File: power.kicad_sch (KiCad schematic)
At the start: 13 parts, among them J2 USB_C_Receptacle_PowerOnly_6P

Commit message: Add files via upload
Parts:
- C1, C2, C3, C4: footprint (none) -> Capacitor_SMD:C_0805_2012Metric
- D2: footprint (none) -> LED_SMD:LED_0805_2012Metric
- R1, R2: footprint (none) -> Resistor_SMD:R_0603_1608Metric
- R3: footprint (none) -> Resistor_SMD:R_0805_2012Metric
- R4: value 2K -> 1.5K; footprint (none) -> Resistor_SMD:R_0805_2012Metric
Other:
- moved on the sheet: D2, R4
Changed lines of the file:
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@@
 	(wire
 		(pts
-			(xy 130.81 90.17) (xy 132.08 90.17)
+			(xy 130.81 69.85) (xy 132.08 69.85)
 		)
 		(stroke
@@
 	(wire
 		(pts
-			(xy 147.32 66.04) (xy 147.32 90.17)
+			(xy 147.32 66.04) (xy 147.32 69.85)
 		)
 		(stroke
@@
 	(wire
 		(pts
-			(xy 130.81 67.31) (xy 130.81 90.17)
+			(xy 130.81 67.31) (xy 130.81 69.85)
 		)
 		(stroke
@@
 			)
 		)
-		(property "Footprint" ""
+		(property "Footprint" "Capacitor_SMD:C_0805_2012Metric"
 			(at 156.21 65.0748 0)
 			(effects
@@
 	(symbol
 		(lib_id "Device:R")
-		(at 135.89 90.17 90)
+		(at 135.89 69.85 90)
 		(unit 1)
 		(exclude_from_sim no)
@@
 		(fields_autoplaced yes)
 		(property "Reference" "R4"
-			(at 135.89 83.82 90)
-			(effects
-				(font
-					(size 1.27 1.27)
-				)
-			)
-		)
-		(property "Value" "2K"
-			(at 135.89 86.36 90)
-			(effects
-				(font
-					(size 1.27 1.27)
-				)
-			)
-		)
-		(property "Footprint" ""
-			(at 135.89 91.948 90)
+			(at 135.89 63.5 90)
+			(effects
+				(font
+					(size 1.27 1.27)
+				)
+			)
+		)
+		(property "Value" "1.5K"
+			(at 135.89 66.04 90)
+			(effects
+				(font
+					(size 1.27 1.27)
+				)
+			)
+		)
+		(property "Footprint" "Resistor_SMD:R_0805_2012Metric"
+			(at 135.89 71.628 90)
 			(effects
 				(font
@@
 		)
 		(property "Datasheet" "~"
-			(at 135.89 90.17 0)
+			(at 135.89 69.85 0)
 			(effects
 				(font
@@
 		)
 		(property "Description" "Resistor"
-			(at 135.89 90.17 0)
+			(at 135.89 69.85 0)
 			(effects
 				(font
@@
 			)
 		)
-		(property "Footprint" ""
+		(property "Footprint" "Resistor_SMD:R_0805_2012Metric"
 			(at 111.252 60.96 90)
 			(effects
@@
 			)
 		)
-		(property "Footprint" ""
+		(property "Footprint" "Resistor_SMD:R_0603_1608Metric"
 			(at 139.7 46.228 90)
 			(effects
@@
 			)
 		)
-		(property "Footprint" ""
+		(property "Footprint" "Capacitor_SMD:C_0805_2012Metric"
 			(at 156.21 59.9948 0)
 			(effects
@@
 			)
 		)
-		(property "Footprint" ""
+		(property "Footprint" "Capacitor_SMD:C_0805_2012Metric"
 			(at 156.21 37.1348 0)
 			(effects
@@
 			)
 		)
-		(property "Footprint" ""
+		(property "Footprint" "Capacitor_SMD:C_0805_2012Metric"
 			(at 156.21 43.4848 0)
 			(effects
@@
 			)
 		)
-		(property "Footprint" ""
+		(property "Footprint" "Resistor_SMD:R_0603_1608Metric"
 			(at 139.7 48.768 90)
 			(effects
@@
 	(symbol
 		(lib_id "Device:LED")
-		(at 143.51 90.17 0)
+		(at 143.51 69.85 0)
 		(unit 1)
 		(exclude_from_sim no)
@@
 		(fields_autoplaced yes)
 		(property "Reference" "D2"
-			(at 141.9225 83.82 0)
+			(at 141.9225 63.5 0)
 			(effects
 				(font
@@
 		)
 		(property "Value" "LED"
-			(at 141.9225 86.36 0)
-			(effects
-				(font
-					(size 1.27 1.27)
-				)
-			)
-		)
-		(property "Footprint" ""
-			(at 143.51 90.17 0)
+			(at 141.9225 66.04 0)
+			(effects
+				(font
+					(size 1.27 1.27)
+				)
+			)
+		)
+		(property "Footprint" "LED_SMD:LED_0805_2012Metric"
+			(at 143.51 69.85 0)
 			(effects
 				(font
@@
 		)
 		(property "Datasheet" "~"
-			(at 143.51 90.17 0)
+			(at 143.51 69.85 0)
 			(effects
 				(font
@@
 		)
 		(property "Description" "Light emitting diode"
-			(at 143.51 90.17 0)
+			(at 143.51 69.85 0)
 			(effects
 				(font
@@
 		)
 		(property "Sim.Pins" "1=K 2=A"
-			(at 143.51 90.17 0)
-			(effects
-				(font
+			(at 143.51 69.85 0)
+			(effects
+				(font

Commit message: Add files via upload
v1.2 : complete schematics with added footprints, PCB layout remaining
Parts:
- added TP_3V3, TP_VBUS1, TP_gnd1: TestPoint, TestPoint:TestPoint_Pad_D1.5mm, symbol Connector:TestPoint
- F1: footprint (none) -> Fuse:Fuse_1206_3216Metric
- J2: footprint (none) -> Connector_USB:USB_C_Receptacle_HRO_TYPE-C-31-M-12
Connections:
- net GND: now also TP_gnd1.1
- net VBUS_5V: now also TP_VBUS1.1
- net Vlogic_3V3: now also TP_3V3.1
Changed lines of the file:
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@@
+	)
+	(junction
+		(at 147.32 69.85)
+		(diameter 0)
+		(color 0 0 0 0)
 	)
 	(junction
@@
 	)
 	(junction
+		(at 120.65 58.42)
+		(diameter 0)
+		(color 0 0 0 0)
+	)
+	(junction
 		(at 156.21 60.96)
 		(diameter 0)
@@
 	)
 	(junction
+		(at 146.05 31.75)
+		(diameter 0)
+		(color 0 0 0 0)
+	)
+	(junction
 		(at 156.21 44.45)
 		(diameter 0)
@@
 	(wire
 		(pts
+			(xy 120.65 58.42) (xy 120.65 57.15)
+		)
+		(stroke
+			(width 0)
+			(type default)
+		)
+	)
+	(wire
+		(pts
 			(xy 156.21 38.1) (xy 156.21 44.45)
 		)
@@
 	(wire
 		(pts
+			(xy 146.05 31.75) (xy 148.59 31.75)
+		)
+		(stroke
+			(width 0)
+			(type default)
+		)
+	)
+	(wire
+		(pts
 			(xy 147.32 66.04) (xy 147.32 69.85)
 		)
@@
 	(wire
 		(pts
-			(xy 143.51 31.75) (xy 148.59 31.75)
+			(xy 143.51 31.75) (xy 146.05 31.75)
 		)
 		(stroke
@@
 	(wire
 		(pts
-			(xy 120.65 60.96) (xy 120.65 57.15)
+			(xy 120.65 60.96) (xy 120.65 58.42)
 		)
 		(stroke
@@
 	)
 	(symbol
+		(lib_id "Connector:TestPoint")
+		(at 146.05 31.75 180)
+		(unit 1)
+		(exclude_from_sim no)
+		(in_bom yes)
+		(on_board yes)
+		(dnp no)
+		(fields_autoplaced yes)
+		(property "Reference" "TP_VBUS1"
+			(at 148.59 33.7819 0)
+			(effects
+				(font
+					(size 1.27 1.27)
+				)
+				(justify right)
+			)
+		)
+		(property "Value" "TestPoint"
+			(at 148.59 36.3219 0)
+			(effects
+				(font
+					(size 1.27 1.27)
+				)
+				(justify right)
+			)
+		)
+		(property "Footprint" "TestPoint:TestPoint_Pad_D1.5mm"
+			(at 140.97 31.75 0)
+			(effects
+				(font
+					(size 1.27 1.27)
+				)
+				(hide yes)
+			)
+		)
+		(property "Datasheet" "~"
+			(at 140.97 31.75 0)
+			(effects
+				(font
+					(size 1.27 1.27)
+				)
+				(hide yes)
+			)
+		)
+		(property "Description" "test point"
+			(at 146.05 31.75 0)
+			(effects
+				(font
+					(size 1.27 1.27)
+				)
+				(hide yes)
+			)
+		)
+		(pin "1"
+		)
+		(instances
+			(project ""
+				(path "/c8d0e3cf-b697-430c-b4f3-c5285558b4ca/a3d1f251-0cce-4493-9b12-767abad6ca7c"
+					(reference "TP_VBUS1")
+					(unit 1)
+				)
+			)
+		)
+	)
+	(symbol
 		(lib_id "Device:R")
 		(at 113.03 60.96 0)
@@
 			)
 		)
-		(property "Footprint" ""
+		(property "Footprint" "Connector_USB:USB_C_Receptacle_HRO_TYPE-C-31-M-12"
 			(at 124.46 36.83 0)
 			(effects
@@
 			)
 		)
-		(property "Footprint" ""
+		(property "Footprint" "Fuse:Fuse_1206_3216Metric"
 			(at 144.78 30.48 0)
 			(effects
@@
 					(unit 1)
 				)
+			)
+		)
+	)
+	(symbol
+		(lib_id "Connector:TestPoint")
+		(at 147.32 69.85 270)
+		(unit 1)
+		(exclude_from_sim no)
+		(in_bom yes)
+		(on_board yes)
+		(dnp no)
+		(fields_autoplaced yes)
+		(property "Reference" "TP_3V3"
+			(at 152.4 68.5799 90)
+			(effects
+				(font
+					(size 1.27 1.27)
+				)
+				(justify left)
+			)
+		)
+		(property "Value" "TestPoint"
+			(at 152.4 71.1199 90)
+			(effects
+				(font
+					(size 1.27 1.27)
+				)
+				(justify left)
+			)
+		)
+		(property "Footprint" "TestPoint:TestPoint_Pad_D1.5mm"
+			(at 147.32 74.93 0)
+			(effects
+				(font
+					(size 1.27 1.27)
+				)
+				(hide yes)
+			)
+		)
+		(property "Datasheet" "~"
+			(at 147.32 74.93 0)
+			(effects
+				(font
+					(size 1.27 1.27)
+				)
+				(hide yes)
+			)
+		)
+		(property "Description" "test point"
+			(at 147.32 69.85 0)
+			(effects
+				(font
+					(size 1.27 1.27)
+				)
+				(hide yes)
+			)
+		)
+		(pin "1"
+		)
+		(instances
+			(project ""
+				(path "/c8d0e3cf-b697-430c-b4f3-c5285558b4ca/a3d1f251-0cce-4493-9b12-767abad6ca7c"
+					(reference "TP_3V3")
+					(unit 1)
+				)
+			)
+		)
+	)
+	(symbol
+		(lib_id "Connector:TestPoint")
+		(at 120.65 58.42 270)
+		(unit 1)
+		(exclude_from_sim no)
+		(in_bom yes)
+		(on_board yes)
+		(dnp no)
+		(fields_autoplaced yes)
+		(property "Reference" "TP_gnd1"
+			(at 125.73 57.1499 90)
+			(effects
+				(font
+					(size 1.27 1.27)
+				)
+				(justify left)
+			)
+		)
+		(property "Value" "TestPoint"
+			(at 125.73 59.6899 90)
+			(effects
+				(font
+					(size 1.27 1.27)
+				)
+				(justify left)
+			)
+		)
+		(property "Footprint" "TestPoint:TestPoint_Pad_D1.5mm"
+			(at 120.65 63.5 0)
+			(effects
+				(font
+					(size 1.27 1.27)
+				)
+				(hide yes)
+			)
+		)
+		(property "Datasheet" "~"
+			(at 120.65 63.5 0)
+			(effects
+				(font
+					(size 1.27 1.27)
+				)
+				(hide yes)
+			)
+		)
+		(property "Description" "test point"
+			(at 120.65 58.42 0)
+			(effects
+				(font
+					(size 1.27 1.27)
+				)
+				(hide yes)
+			)
+		)
+		(pin "1"
+		)
+		(instances
+			(project ""
+				(path "/c8d0e3cf-b697-430c-b4f3-c5285558b4ca/a3d1f251-0cce-4493-9b12-767abad6ca7c"
+					(reference "TP_gnd1")
+					(unit 1)
+				)

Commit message: Add files via upload
v3 : almost complete PCB layout, one common GND instance missing, USB-C footprint without BOM
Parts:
- J2: footprint Connector_USB:USB_C_Receptacle_HRO_TYPE-C-31-M-12 -> Connector_USB:USB_C_Receptacle_HRO_TYPE-C-31-M-17
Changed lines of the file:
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@@
 			)
 		)
-		(property "Footprint" "Connector_USB:USB_C_Receptacle_HRO_TYPE-C-31-M-12"
+		(property "Footprint" "Connector_USB:USB_C_Receptacle_HRO_TYPE-C-31-M-17"
 			(at 124.46 36.83 0)
 			(effects

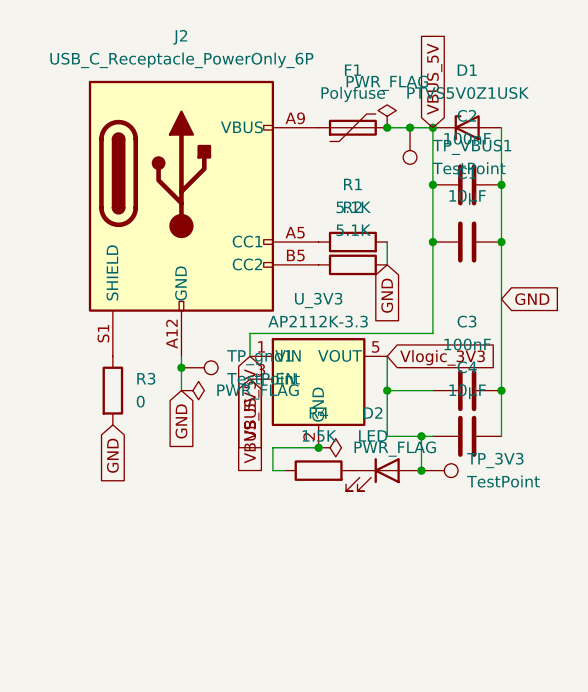
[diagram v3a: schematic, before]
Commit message: Add files via upload
V4 : completed and working PCB. now zero DRC errors yet. room for refinement but working.
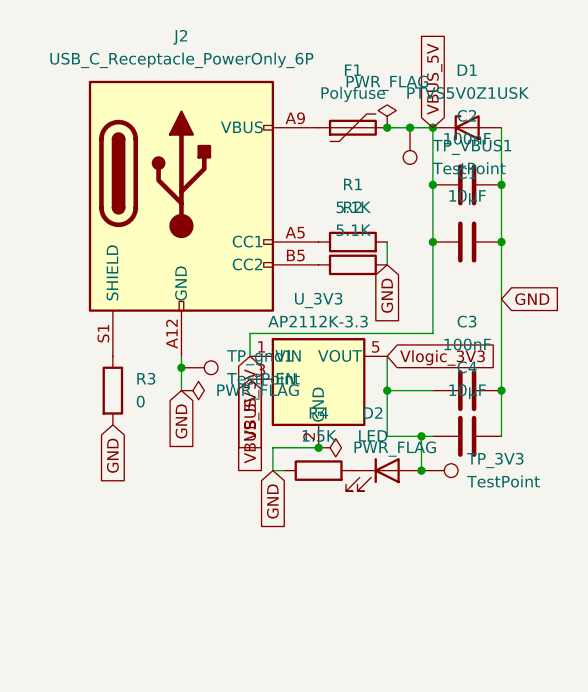
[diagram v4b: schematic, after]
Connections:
- net GND: now also R4.1, U_3V3.2 (GND)
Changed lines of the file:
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@@
+		)
+	)
+	(global_label "GND"
+		(shape input)
+		(at 130.81 69.85 270)
+		(fields_autoplaced yes)
+		(effects
+			(font
+				(size 1.27 1.27)
+			)
+			(justify right)
+		)
+		(property "Intersheetrefs" "${INTERSHEET_REFS}"
+			(at 130.81 76.7057 90)
+			(effects
+				(font
+					(size 1.27 1.27)
+				)
+				(justify right)
+				(hide yes)
+			)
 		)
 	)

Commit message: Add files via upload
V4 : full and final v1.1. Working schematics. Working PCB layout, zero ERC and DRC errors and warnings(except for cosmetic ones).
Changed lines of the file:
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@@
-	)
-	(symbol
-		(lib_id "power:PWR_FLAG")
-		(at 120.65 60.96 270)
-		(unit 1)
-		(exclude_from_sim no)
-		(in_bom yes)
-		(on_board yes)
-		(dnp no)
-		(fields_autoplaced yes)
-		(property "Reference" "#FLG02"
-			(at 122.555 60.96 0)
-			(effects
-				(font
-					(size 1.27 1.27)
-				)
-				(hide yes)
-			)
-		)
-		(property "Value" "PWR_FLAG"
-			(at 124.46 60.9599 90)
-			(effects
-				(font
-					(size 1.27 1.27)
-				)
-				(justify left)
-			)
-		)
-		(property "Footprint" ""
-			(at 120.65 60.96 0)
-			(effects
-				(font
-					(size 1.27 1.27)
-				)
-				(hide yes)
-			)
-		)
-		(property "Datasheet" "~"
-			(at 120.65 60.96 0)
-			(effects
-				(font
-					(size 1.27 1.27)
-				)
-				(hide yes)
-			)
-		)
-		(property "Description" "Special symbol for telling ERC where power comes from"
-			(at 120.65 60.96 0)
-			(effects
-				(font
-					(size 1.27 1.27)
-				)
-				(hide yes)
-			)
-		)
-		(pin "1"
-		)
-		(instances
-			(project ""
-				(path "/c8d0e3cf-b697-430c-b4f3-c5285558b4ca/a3d1f251-0cce-4493-9b12-767abad6ca7c"
-					(reference "#FLG02")
-					(unit 1)
-				)
-			)
-		)
 	)
 	(symbol

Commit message: Add files via upload
V5 : complete finish for v1, directly to-the-fab design.
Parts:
- C1, C4: LCSC (none) -> C15850
- C2, C3: LCSC (none) -> C49678
- D1: LCSC (none) -> C85364
- D2: LCSC (none) -> C2827270
- F1: LCSC (none) -> C70059
- J2: LCSC (none) -> C283540
- R1, R2: LCSC (none) -> C23186
- R3: LCSC (none) -> C17477
- R4: value 1.5K -> 1K; LCSC (none) -> C17604
- TP_3V3, TP_VBUS1, TP_gnd1: now left out of the parts list
- U_3V3: LCSC (none) -> C51118
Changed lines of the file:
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@@
+			)
+		)
+		(property "LCSC" "C85364"
+			(at 152.4 31.75 0)
+			(effects
+				(font
+					(size 1.27 1.27)
+				)
+				(hide yes)
 			)
 		)
@@
 			)
 		)
+		(property "LCSC" "C15850"
+			(at 152.4 66.04 90)
+			(effects
+				(font
+					(size 1.27 1.27)
+				)
+				(hide yes)
+			)
+		)
 		(pin "1"
 		)
@@
 			)
 		)
-		(property "Value" "1.5K"
+		(property "Value" "1K"
 			(at 135.89 66.04 90)
 			(effects
@@
 			)
 		)
+		(property "LCSC" "C17604"
+			(at 135.89 69.85 90)
+			(effects
+				(font
+					(size 1.27 1.27)
+				)
+				(hide yes)
+			)
+		)
 		(pin "1"
 		)
@@
 			)
 		)
+		(property "LCSC" "C51118"
+			(at 135.89 59.69 0)
+			(effects
+				(font
+					(size 1.27 1.27)
+				)
+				(hide yes)
+			)
+		)
 		(pin "1"
 		)
@@
 		(unit 1)
 		(exclude_from_sim no)
-		(in_bom yes)
+		(in_bom no)
 		(on_board yes)
 		(dnp no)
@@
 			)
 		)
+		(property "LCSC" ""
+			(at 146.05 31.75 0)
+			(effects
+				(font
+					(size 1.27 1.27)
+				)
+				(hide yes)
+			)
+		)
 		(pin "1"
 		)
@@
 			)
 		)
+		(property "LCSC" "C17477"
+			(at 113.03 60.96 0)
+			(effects
+				(font
+					(size 1.27 1.27)
+				)
+				(hide yes)
+			)
+		)
 		(pin "2"
 		)
@@
 			)
 		)
+		(property "LCSC" "C23186"
+			(at 139.7 44.45 90)
+			(effects
+				(font
+					(size 1.27 1.27)
+				)
+				(hide yes)
+			)
+		)
 		(pin "2"
 		)
@@
 			)
 		)
+		(property "LCSC" "C49678"
+			(at 152.4 60.96 90)
+			(effects
+				(font
+					(size 1.27 1.27)
+				)
+				(hide yes)
+			)
+		)
 		(pin "1"
 		)
@@
 			)
 		)
+		(property "LCSC" "C49678"
+			(at 152.4 38.1 90)
+			(effects
+				(font
+					(size 1.27 1.27)
+				)
+				(hide yes)
+			)
+		)
 		(pin "2"
 		)
@@
 			)
 		)
+		(property "LCSC" "C283540"
+			(at 120.65 39.37 0)
+			(effects
+				(font
+					(size 1.27 1.27)
+				)
+				(hide yes)
+			)
+		)
 		(pin "B12"
 		)
@@
 			)
 		)
+		(property "LCSC" "C15850"
+			(at 152.4 44.45 90)
+			(effects
+				(font
+					(size 1.27 1.27)
+				)
+				(hide yes)
+			)
+		)
 		(pin "1"
 		)
@@
 			)
 		)
+		(property "LCSC" "C23186"
+			(at 139.7 46.99 90)
+			(effects
+				(font
+					(size 1.27 1.27)
+				)
+				(hide yes)
+			)
+		)
 		(pin "2"
 		)
@@
 			)
 		)
+		(property "LCSC" "C2827270"
+			(at 143.51 69.85 0)
+			(effects
+				(font
+					(size 1.27 1.27)
+				)
+				(hide yes)
+			)
+		)
 		(pin "2"
 		)
@@
 			)
 		)
+		(property "LCSC" "C70059"
+			(at 139.7 31.75 90)
+			(effects
+				(font
+					(size 1.27 1.27)
+				)
+				(hide yes)
+			)
+		)
 		(pin "1"
 		)
@@
 		(unit 1)
 		(exclude_from_sim no)
-		(in_bom yes)
+		(in_bom no)
 		(on_board yes)
 		(dnp no)
@@
 			)
 		)
+		(property "LCSC" ""
+			(at 147.32 69.85 90)
+			(effects
+				(font
+					(size 1.27 1.27)
+				)
+				(hide yes)
+			)
+		)
 		(pin "1"
 		)
@@
 		(unit 1)
 		(exclude_from_sim no)
-		(in_bom yes)
+		(in_bom no)
 		(on_board yes)
 		(dnp no)
@@
 			(effects
 				(font
+					(size 1.27 1.27)
+				)
+				(hide yes)
+			)
+		)
+		(property "LCSC" ""
+			(at 120.65 58.42 90)
+			(effects
+				(font
